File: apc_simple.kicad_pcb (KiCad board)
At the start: 2 copper layers, 16 parts, among them J1 Output, U1 NE556

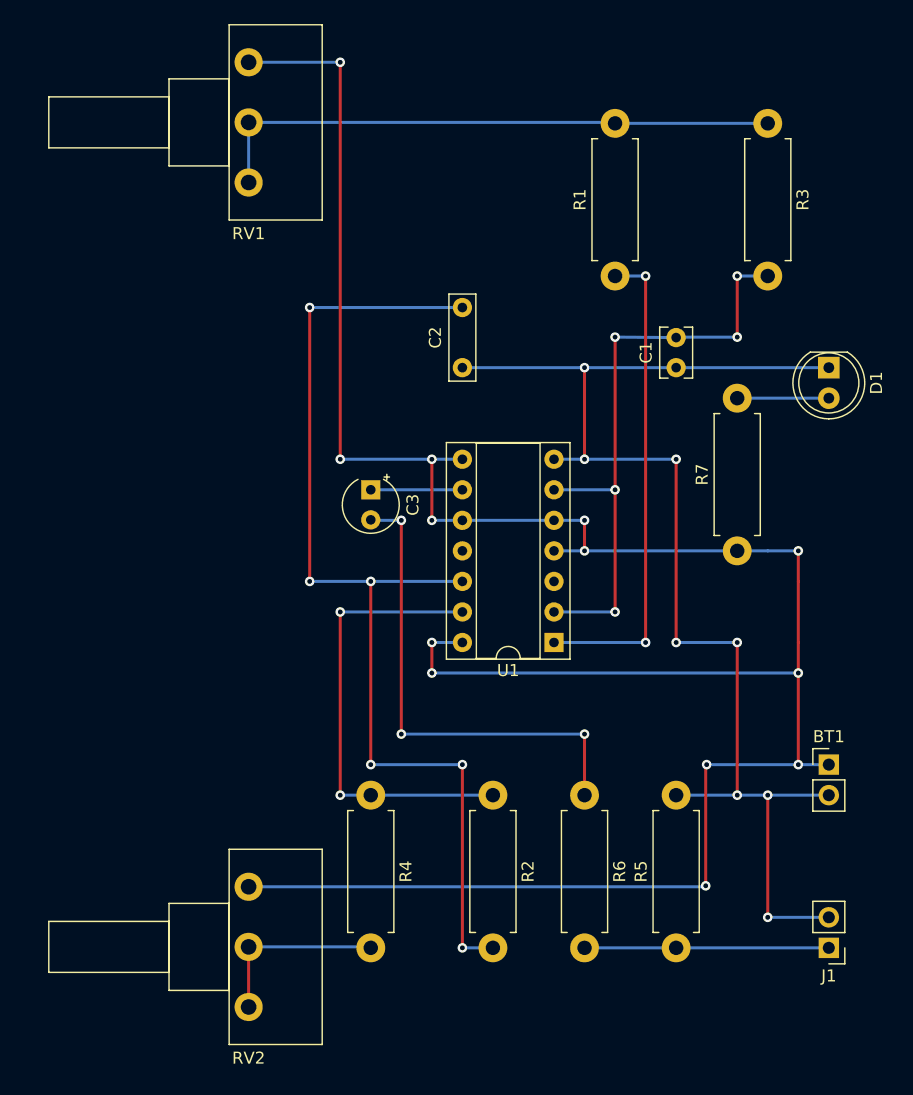
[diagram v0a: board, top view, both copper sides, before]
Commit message: Fixed error in schematic; re-designed breadboard wiring
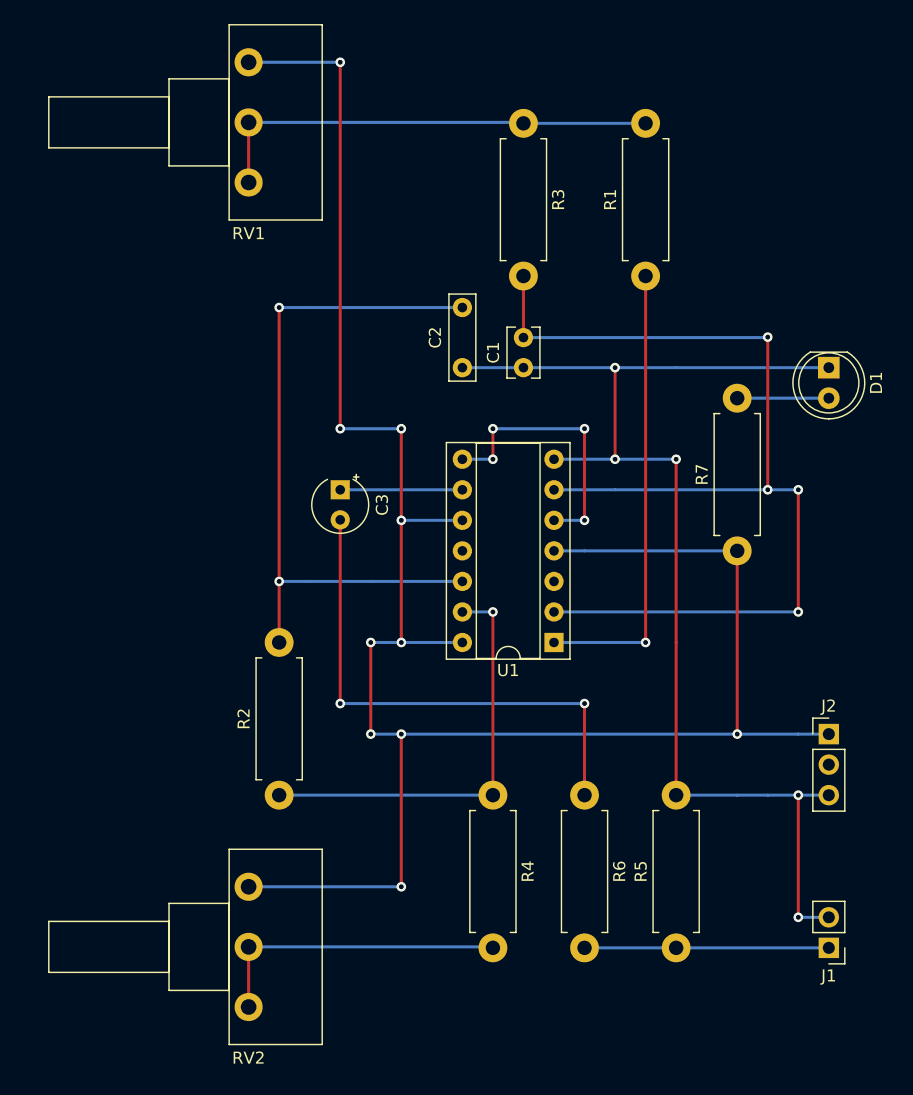
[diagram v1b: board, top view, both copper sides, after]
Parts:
- removed BT1: Battery_Cell, Connector_PinHeader_2.54mm:PinHeader_1x02_P2.54mm_Vertical
- added J2: Power, Connector_PinHeader_2.54mm:PinHeader_1x03_P2.54mm_Vertical, F.Cu at (162.6, 109.2)
- moved R3 20.3 mm to (137.2, 58.4)
- moved R2 17.8 mm to (116.8, 114.3), turned to 90 degrees
- moved C1 12.7 mm to (137.2, 78.7)
- moved R4 10.2 mm to (134.6, 114.3)
- moved C3 2.54 mm to (121.9, 88.9)
- moved R1 2.54 mm to (147.3, 71.1)
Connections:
- U1 pad 5: +5V -> Net-(U1-Pad5)
- U1 pad 8: +5V -> Net-(U1-Pad5)
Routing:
- net Net-(C1-Pad2): track 50.8 -> 89.0 mm, vias 5 -> 4
- net Net-(C2-Pad2): track 88.9 -> 58.3 mm, vias 7 -> 2
- net +5V: track 203.0 -> 175.1 mm, vias 13 -> 10
- net Net-(U1-Pad5): track 0.00 -> 22.9 mm, vias 0 -> 4
- net Net-(R1-Pad2): track 48.2 -> 38.1 mm
- net Net-(R4-Pad2): track 15.4 -> 25.4 mm
- net GND: track 109.3 -> 101.7 mm, vias 8 -> 5
- net Net-(C3-Pad2): track 40.6 -> 43.2 mm, vias 3 -> 2
- net Net-(R2-Pad1): track 38.1 -> 35.6 mm, vias 2 -> 1
- net Net-(R1-Pad1): track 40.6 -> 38.1 mm, vias 2 -> 1
- net Net-(C3-Pad1): track 7.62 -> 10.2 mm

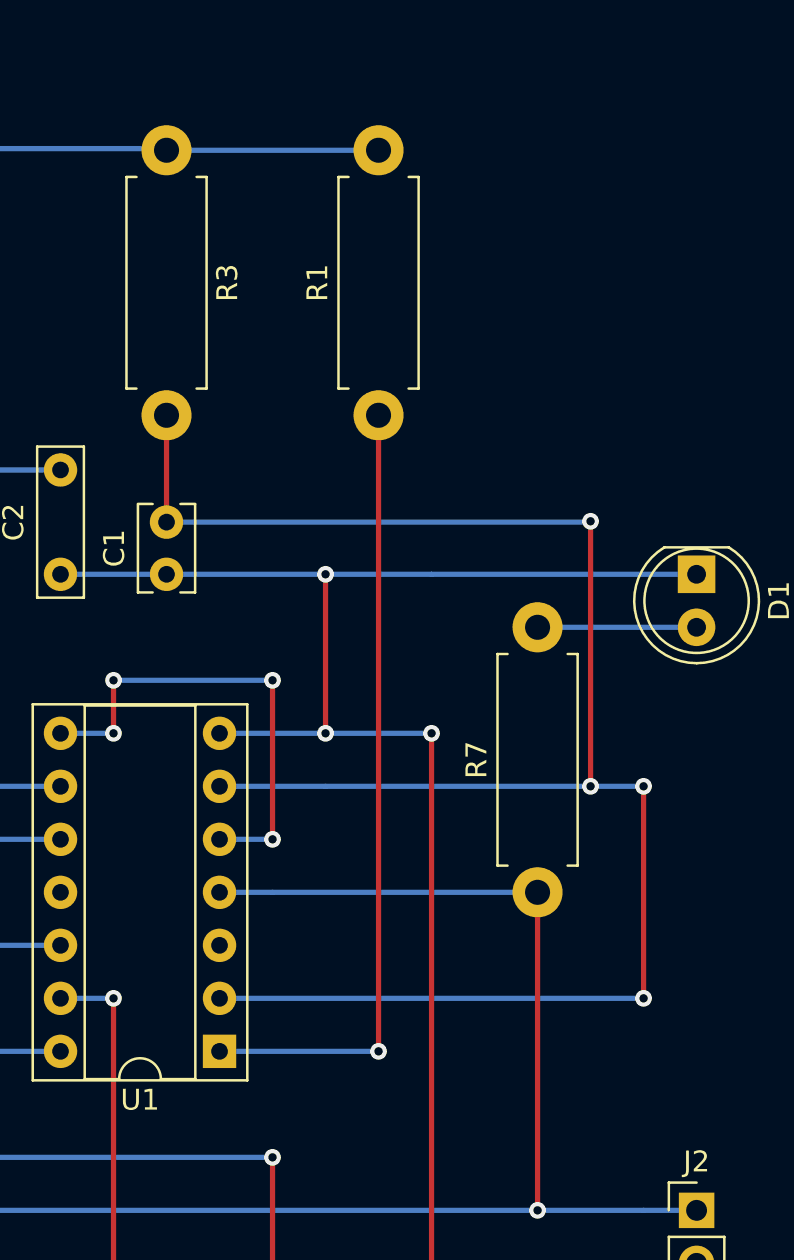
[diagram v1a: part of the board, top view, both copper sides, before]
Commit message: Rewire 1k resistor directly between THR and DIS
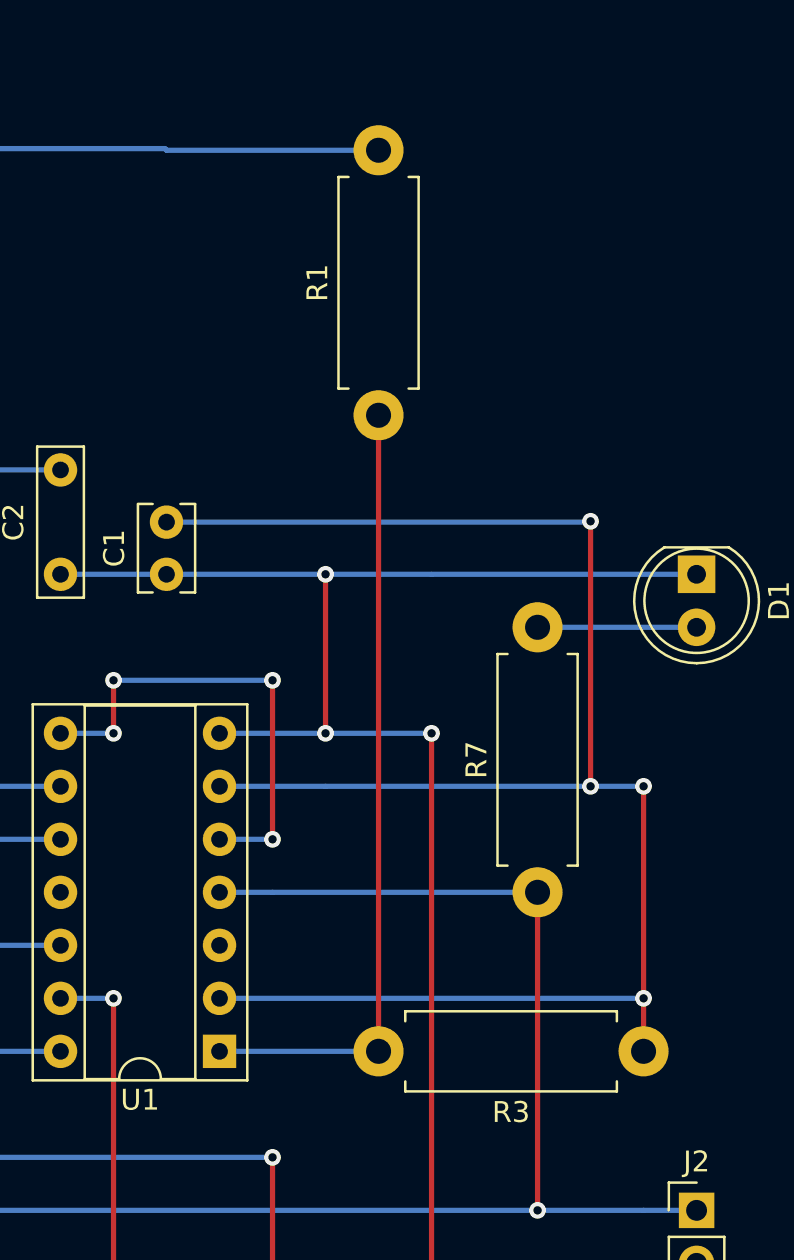
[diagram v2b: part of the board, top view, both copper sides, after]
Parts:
- moved R3 48.9 mm to (160.0, 101.6), turned to 180 degrees
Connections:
- R3 pad 1: Net-(R1-Pad2) -> Net-(C1-Pad2)
- R3 pad 2: Net-(C1-Pad2) -> Net-(R1-Pad1)
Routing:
- net Net-(C1-Pad2): track 89.0 -> 86.4 mm

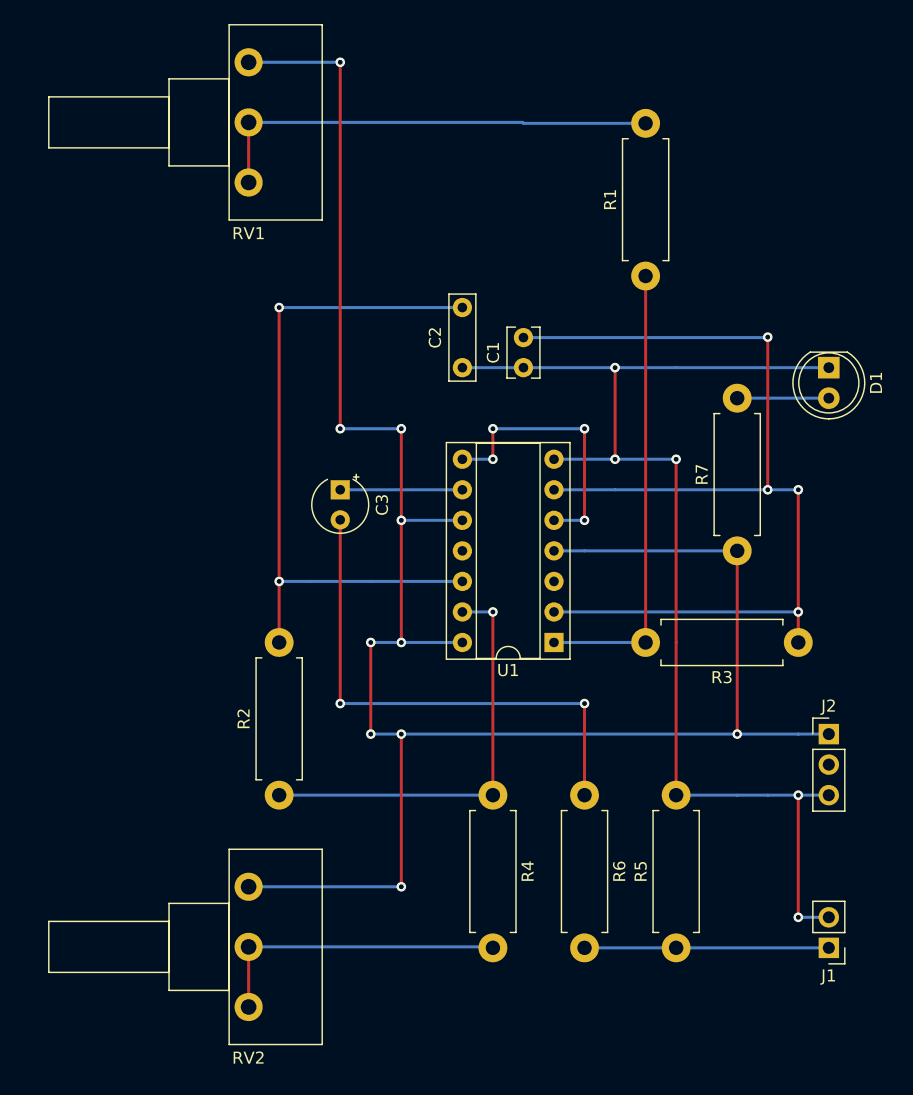
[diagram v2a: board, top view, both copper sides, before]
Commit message: pcb: reroute for strip mask pattern
Adapt some resistor footprints to indicate better
where they are used to bridge connections. Make
every upper layer wire bridge standalone.
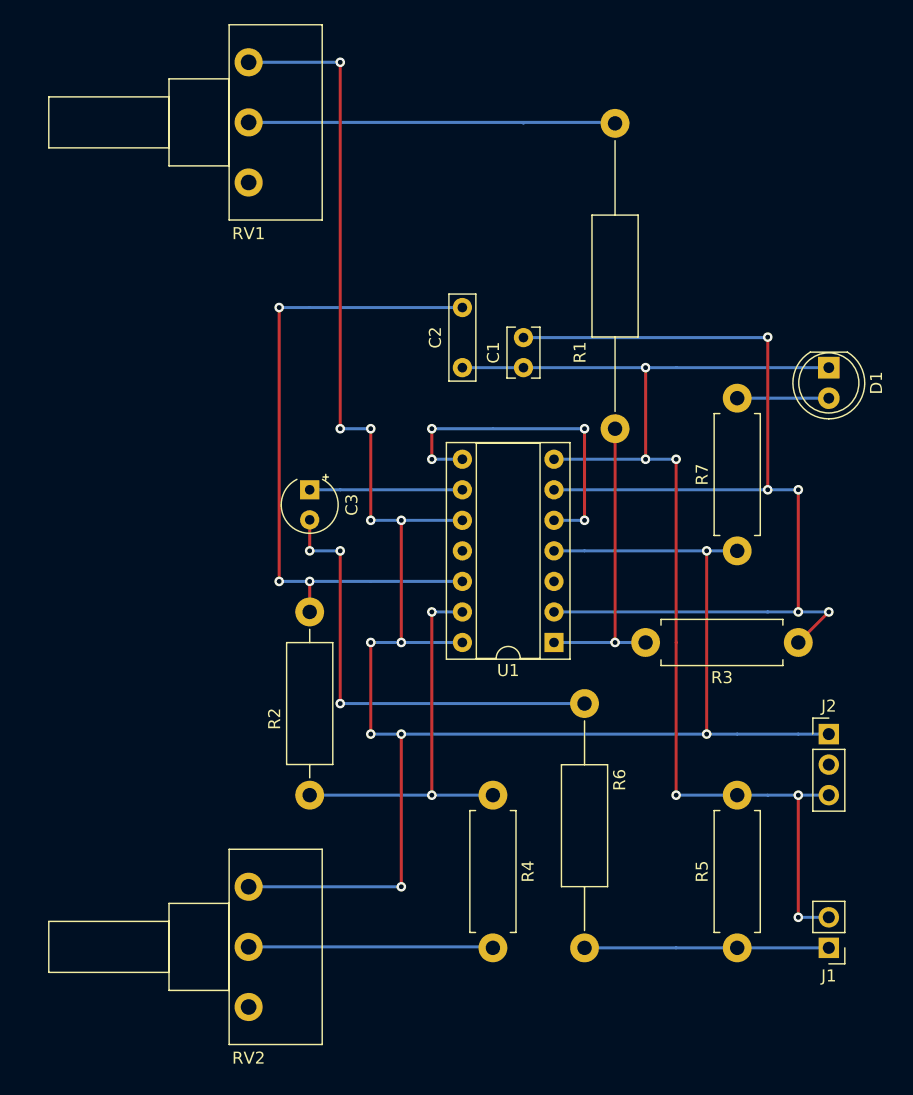
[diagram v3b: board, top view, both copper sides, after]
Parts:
- R1: footprint Resistor_THT:R_Axial_DIN0411_L9.9mm_D3.6mm_P12.70mm_Horizontal -> Resistor_THT:R_Axial_DIN0411_L9.9mm_D3.6mm_P25.40mm_Horizontal
- R2: footprint Resistor_THT:R_Axial_DIN0411_L9.9mm_D3.6mm_P12.70mm_Horizontal -> Resistor_THT:R_Axial_DIN0411_L9.9mm_D3.6mm_P15.24mm_Horizontal
- R6: footprint Resistor_THT:R_Axial_DIN0411_L9.9mm_D3.6mm_P12.70mm_Horizontal -> Resistor_THT:R_Axial_DIN0411_L9.9mm_D3.6mm_P20.32mm_Horizontal
- moved R1 13.0 mm to (144.8, 83.8)
- moved R6 7.62 mm to (142.2, 106.7)
- moved R5 5.08 mm to (154.9, 127.0)
- moved C3 2.54 mm to (119.4, 88.9)
- moved R2 2.54 mm to (119.4, 114.3)
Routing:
- net Net-(R1-Pad1): track 38.1 -> 25.4 mm
- net Net-(R1-Pad2): track 38.1 -> 30.6 mm
- net Net-(U1-Pad5): track 22.9 -> 27.9 mm
- net Net-(C3-Pad2): track 43.2 -> 38.1 mm, vias 2 -> 4
- net Net-(R4-Pad2): track 25.4 -> 20.4 mm
- net Net-(C1-Pad2): track 86.4 -> 90.0 mm, vias 4 -> 5
- net Net-(C3-Pad1): track 10.2 -> 12.7 mm
- net Net-(C2-Pad2): track 58.3 -> 55.8 mm, vias 2 -> 3
- net Net-(R2-Pad1): track 35.6 -> 33.0 mm, vias 1 -> 2
- net GND: vias 5 -> 6
- net +5V: vias 10 -> 12

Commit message: Make it fit 19x19 strip mask
Switch around some connectors and footprints.
Mark strip mask lane cutting marks on backside "silk screen".
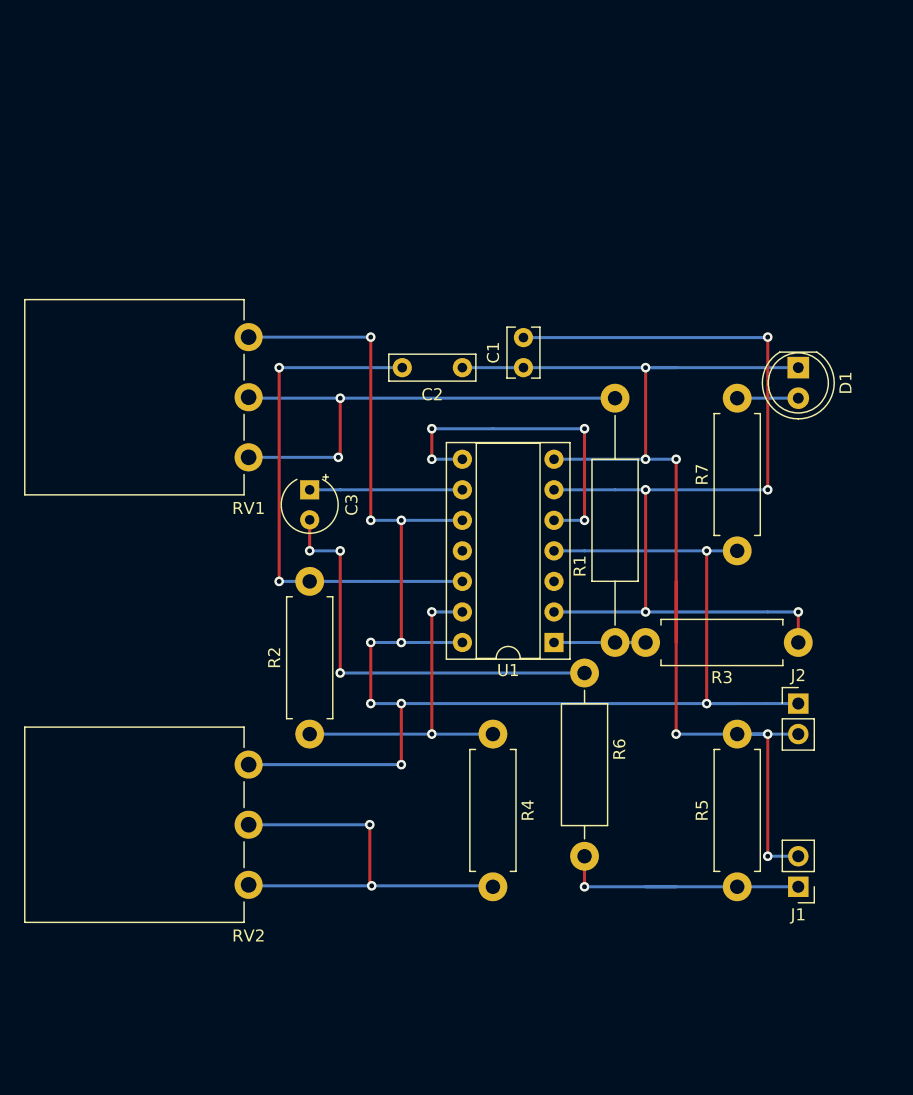
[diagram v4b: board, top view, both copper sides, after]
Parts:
- J2: footprint Connector_PinHeader_2.54mm:PinHeader_1x03_P2.54mm_Vertical -> Connector_PinHeader_2.54mm:PinHeader_1x02_P2.54mm_Vertical
- R1: footprint Resistor_THT:R_Axial_DIN0411_L9.9mm_D3.6mm_P25.40mm_Horizontal -> Resistor_THT:R_Axial_DIN0411_L9.9mm_D3.6mm_P20.32mm_Horizontal
- R2: footprint Resistor_THT:R_Axial_DIN0411_L9.9mm_D3.6mm_P15.24mm_Horizontal -> Resistor_THT:R_Axial_DIN0411_L9.9mm_D3.6mm_P12.70mm_Horizontal
- R6: footprint Resistor_THT:R_Axial_DIN0411_L9.9mm_D3.6mm_P20.32mm_Horizontal -> Resistor_THT:R_Axial_DIN0411_L9.9mm_D3.6mm_P15.24mm_Horizontal
- RV1, RV2: footprint Potentiometer_THT:Potentiometer_Piher_T-16H_Single_Horizontal -> Potentiometer_THT:Potentiometer_Piher_PC-16_Single_Vertical
- moved RV1 22.9 mm to (114.3, 76.2)
- moved R1 17.8 mm to (144.8, 101.6)
- moved RV2 10.2 mm to (114.3, 111.8)
- moved J1 5.68 mm to (160.0, 121.9)
- moved R2 5.08 mm to (119.4, 109.2)
- moved R4 5.08 mm to (134.6, 109.2)
- moved R5 5.08 mm to (154.9, 121.9)
- moved J2 3.59 mm to (160.0, 106.7)
- moved R6 2.54 mm to (142.2, 104.1)
- moved D1 2.54 mm to (160.0, 78.7)
- turned C2 to 180 degrees
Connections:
- J2 pad 2: Net-(J2-Pad2) -> GND
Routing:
- net +5V: track 175.1 -> 139.7 mm, vias 12 -> 10
- net Net-(R1-Pad1): track 25.4 -> 7.62 mm, vias 1 -> 0
- net Net-(R4-Pad2): track 20.4 -> 35.6 mm, vias 0 -> 2
- net Net-(C2-Pad2): track 55.8 -> 43.3 mm, vias 3 -> 2
- net Net-(R1-Pad2): track 30.6 -> 42.9 mm, vias 0 -> 2
- net Net-(C1-Pad2): track 90.0 -> 83.8 mm
- net Net-(R2-Pad1): track 33.0 -> 27.9 mm
- net Net-(J1-Pad1): track 20.3 -> 22.9 mm, vias 0 -> 1
- net Net-(C3-Pad2): track 38.1 -> 35.6 mm, vias 4 -> 3
- net Net-(D1-Pad2): track 7.62 -> 5.08 mm
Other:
- board text added: "X"
